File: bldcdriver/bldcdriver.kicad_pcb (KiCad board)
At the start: 2 copper layers, 147.3 x 81.3 mm, 2 parts, among them U1 DRV8304HRHAR, U2 STM32F103C8Tx

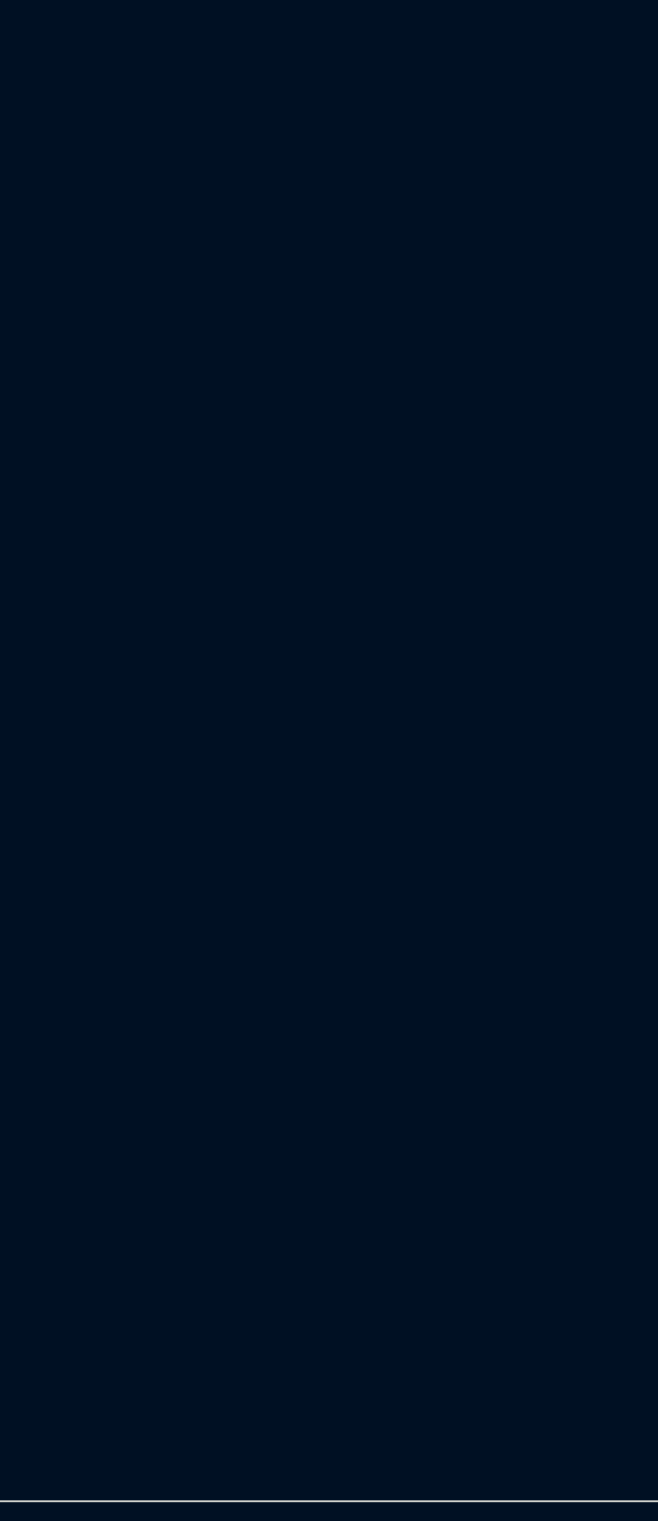
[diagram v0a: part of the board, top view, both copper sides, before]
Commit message: Finished N MOSFET Triple Half Bridge Circuit with Global Labels, looking if I want to use a P MOSFET
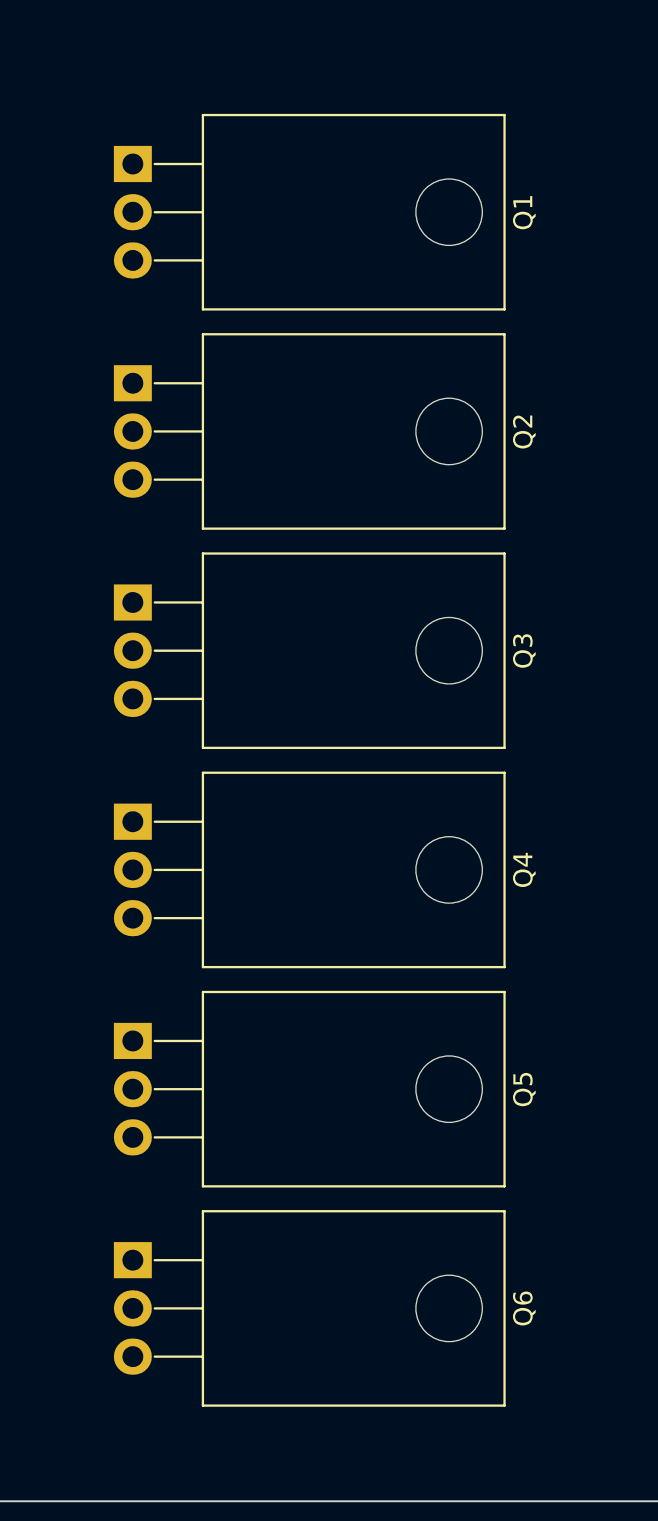
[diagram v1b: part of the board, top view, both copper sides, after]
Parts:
- added Q1: IRF3205, Package_TO_SOT_THT:TO-220-3_Horizontal_TabDown, F.Cu at (135.6, 61.6)
- added Q2: IRF3205, Package_TO_SOT_THT:TO-220-3_Horizontal_TabDown, F.Cu at (135.6, 73.2)
- added Q3: IRF3205, Package_TO_SOT_THT:TO-220-3_Horizontal_TabDown, F.Cu at (135.6, 84.7)
- added Q4: IRF3205, Package_TO_SOT_THT:TO-220-3_Horizontal_TabDown, F.Cu at (135.6, 96.3)
- added Q5: IRF3205, Package_TO_SOT_THT:TO-220-3_Horizontal_TabDown, F.Cu at (135.6, 107.8)
- added Q6: IRF3205, Package_TO_SOT_THT:TO-220-3_Horizontal_TabDown, F.Cu at (135.6, 119.4)
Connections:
- U1 pad 13: unconnected-(U1-GLB-Pad13) -> GLB
- U1 pad 14: unconnected-(U1-SHB-Pad14) -> SHB
- U1 pad 15: unconnected-(U1-GHB-Pad15) -> GHB
- U1 pad 16: unconnected-(U1-GHC-Pad16) -> GHC
- U1 pad 17: unconnected-(U1-SHC-Pad17) -> SHC
- U1 pad 18: unconnected-(U1-GLC-Pad18) -> GLC
- U1 pad 6: unconnected-(U1-GHA-Pad6) -> GHA
- U1 pad 7: unconnected-(U1-SHA-Pad7) -> SHA
- U1 pad 8: unconnected-(U1-GLA-Pad8) -> GLA

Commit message: Few more connections and capacitors
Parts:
- added R1: R, Resistor_SMD:R_0201_0603Metric, F.Cu at (98.7, 100.6)
- added R2: R, Resistor_SMD:R_0201_0603Metric, F.Cu at (98.7, 102.4)
- added R3: R, Resistor_SMD:R_0201_0603Metric, F.Cu at (98.7, 104.1)
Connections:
- net SHA renamed PHASEA
- net SHB renamed PHASEB
- net SHC renamed PHASEC
- Q1 pad 2: unconnected-(Q1-D-Pad2) -> VCC
- Q2 pad 3: unconnected-(Q2-S-Pad3) -> SPA
- Q3 pad 2: unconnected-(Q3-D-Pad2) -> VCC
- Q4 pad 3: unconnected-(Q4-S-Pad3) -> SPB
- Q5 pad 2: unconnected-(Q5-D-Pad2) -> VCC
- Q6 pad 3: unconnected-(Q6-S-Pad3) -> SPC
- U1 pad 1: unconnected-(U1-CPL-Pad1) -> Net-(U1-CPL)
- U1 pad 10: unconnected-(U1-SNA-Pad10) -> SNA
- U1 pad 11: unconnected-(U1-SNB-Pad11) -> SNA
- U1 pad 12: unconnected-(U1-SPB-Pad12) -> SPB
- U1 pad 19: unconnected-(U1-SPC-Pad19) -> SPC
- U1 pad 2: unconnected-(U1-CPH-Pad2) -> Net-(U1-CPH)
- U1 pad 20: unconnected-(U1-SNC-Pad20) -> SNA
- U1 pad 24: unconnected-(U1-VREF-Pad24) -> VCC
- U1 pad 32: unconnected-(U1-AGND-Pad32) -> SNA
- U1 pad 4: unconnected-(U1-VM-Pad4) -> VCC
- U1 pad 40: unconnected-(U1-PGND-Pad40) -> SNA
- U1 pad 41: unconnected-(U1-PAD-Pad41) -> SNA
- U1 pad 5: unconnected-(U1-VDRAIN-Pad5) -> VCC
- U1 pad 9: unconnected-(U1-SPA-Pad9) -> SPA

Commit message: Few changes, not sure
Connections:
- U1 pad 24: VCC -> unconnected-(U1-VREF-Pad24)
- U1 pad 33: unconnected-(U1-DVDD-Pad33) -> +3.3V
- U2 pad 1: unconnected-(U2-VBAT-Pad1) -> VCC
- U2 pad 23: Net-(U2-VSS-Pad23) -> SNA
- U2 pad 24: unconnected-(U2-VDD-Pad24) -> VCC
- U2 pad 35: Net-(U2-VSS-Pad23) -> SNA
- U2 pad 36: unconnected-(U2-VDD-Pad36) -> VCC
- U2 pad 47: Net-(U2-VSS-Pad23) -> SNA
- U2 pad 48: unconnected-(U2-VDD-Pad48) -> VCC
- U2 pad 8: unconnected-(U2-VSSA-Pad8) -> SNA
- U2 pad 9: unconnected-(U2-VDDA-Pad9) -> VCC

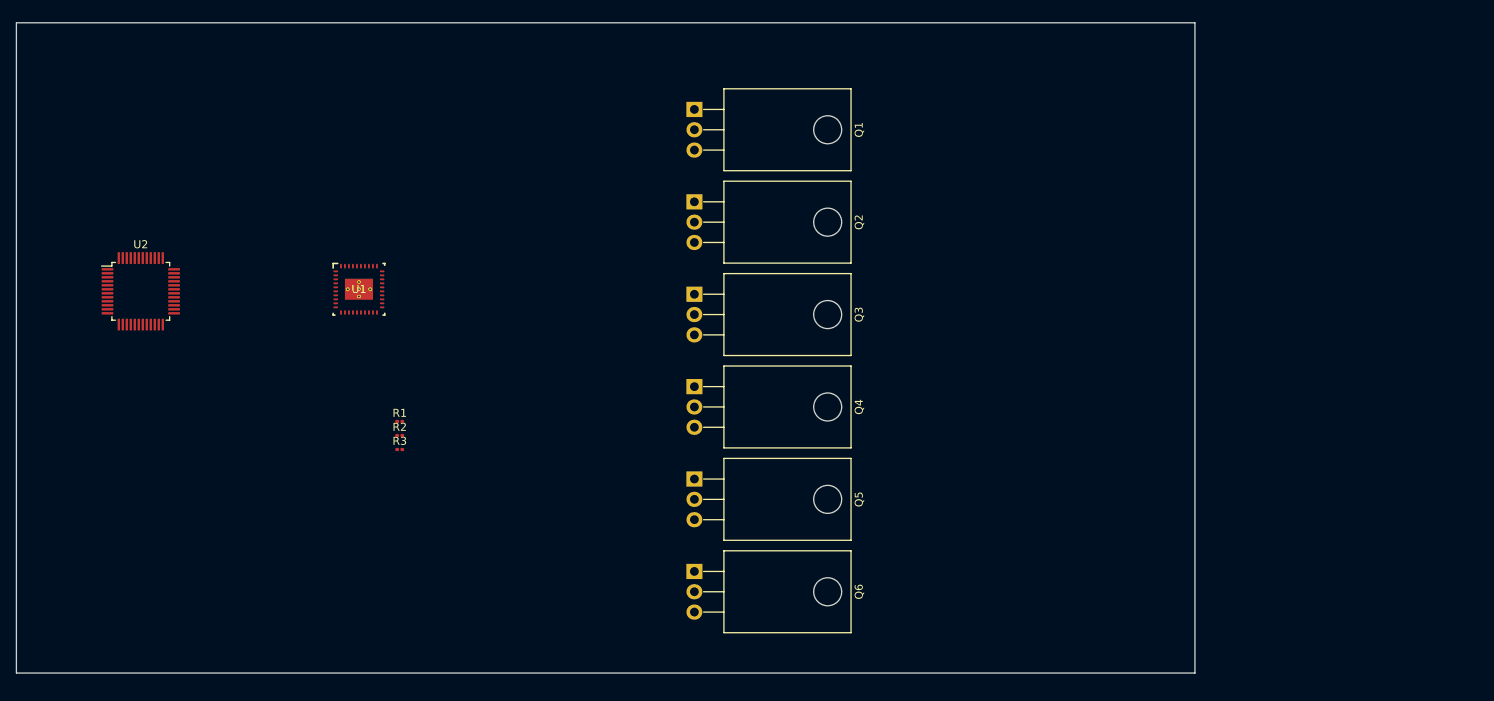
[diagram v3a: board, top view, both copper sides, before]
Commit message: Replaced STM32 with RP2040
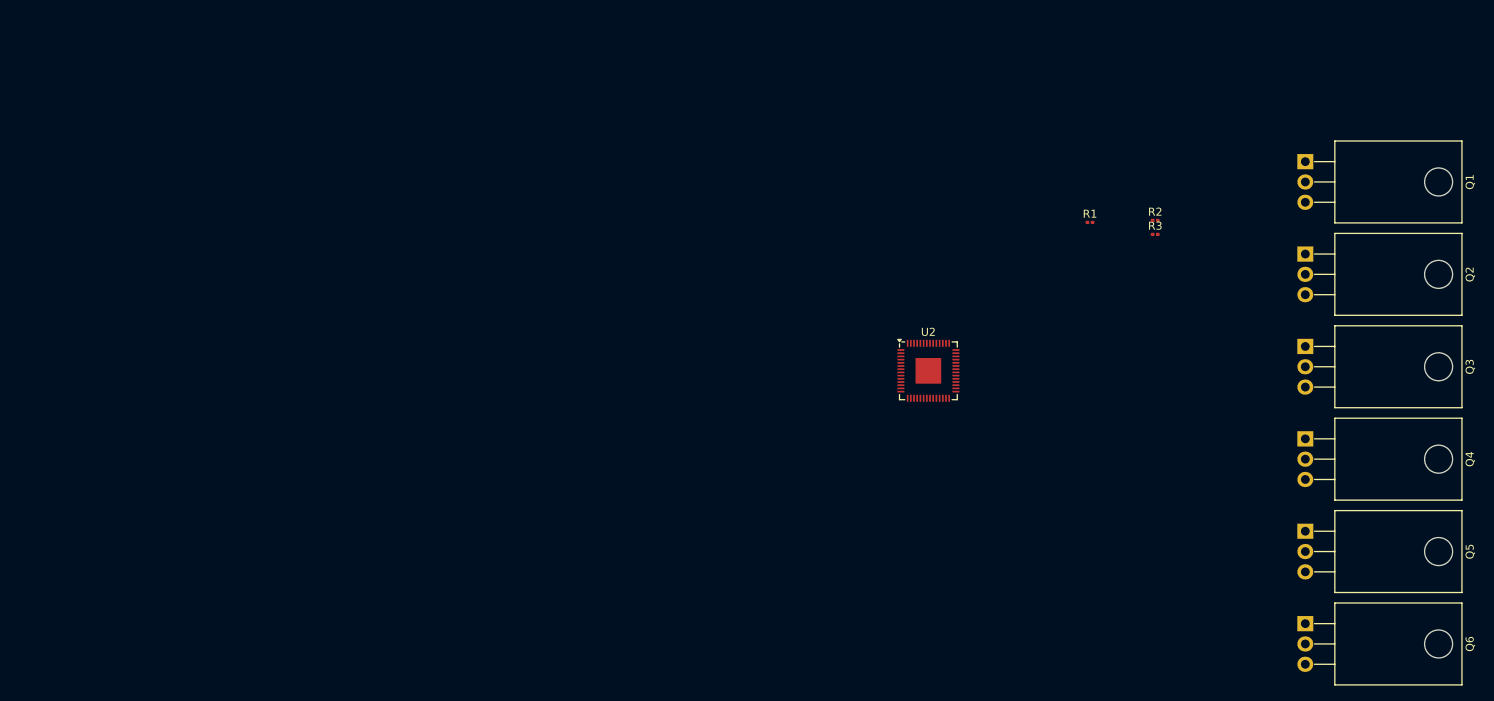
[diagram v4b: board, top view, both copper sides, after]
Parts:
- removed U1: DRV8304HRHAR, DRV8304:RHA0040E
- U2: value STM32F103C8Tx -> RP2040; footprint Package_QFP:LQFP-48_7x7mm_P0.5mm -> Package_DFN_QFN:QFN-56-1EP_7x7mm_P0.4mm_EP3.2x3.2mm
- moved U2 99.0 mm to (164.8, 94.3)
- moved R2 98.2 mm to (193.2, 75.5)
- moved R3 98.2 mm to (193.2, 77.2)
- moved R1 89.8 mm to (185.0, 75.8)
- moved Q1 76.6 mm to (211.9, 68.2)
- moved Q2 76.6 mm to (211.9, 79.7)
- moved Q3 76.6 mm to (211.9, 91.3)
- moved Q4 76.6 mm to (211.9, 102.8)
- moved Q5 76.6 mm to (211.9, 114.4)
- moved Q6 76.6 mm to (211.9, 125.9)
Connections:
- Q1 pad 2: VCC -> +24V
- Q3 pad 2: VCC -> +24V
- Q5 pad 2: VCC -> +24V
- U2 pad 1: VCC -> Net-(U2-IOVDD-Pad1)
- U2 pad 10: unconnected-(U2-PA0-Pad10) -> Net-(U2-IOVDD-Pad1)
- U2 pad 22: unconnected-(U2-PB11-Pad22) -> Net-(U2-IOVDD-Pad1)
- U2 pad 23: SNA -> Net-(U2-DVDD-Pad23)
- U2 pad 24: VCC -> unconnected-(U2-SWCLK-Pad24)
- U2 pad 33: unconnected-(U2-PA12-Pad33) -> Net-(U2-IOVDD-Pad1)
- U2 pad 35: SNA -> unconnected-(U2-GPIO23-Pad35)
- U2 pad 36: VCC -> unconnected-(U2-GPIO24-Pad36)
- U2 pad 42: unconnected-(U2-PB6-Pad42) -> Net-(U2-IOVDD-Pad1)
- U2 pad 47: SNA -> unconnected-(U2-USB_DP-Pad47)
- U2 pad 48: VCC -> unconnected-(U2-USB_VDD-Pad48)
- U2 pad 8: SNA -> unconnected-(U2-GPIO6-Pad8)
- U2 pad 9: VCC -> unconnected-(U2-GPIO7-Pad9)
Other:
- board outline removed

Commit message: Replaced the mistake in symbol from H to S, redid the connections, cleaned up local library folders, added proper net labels
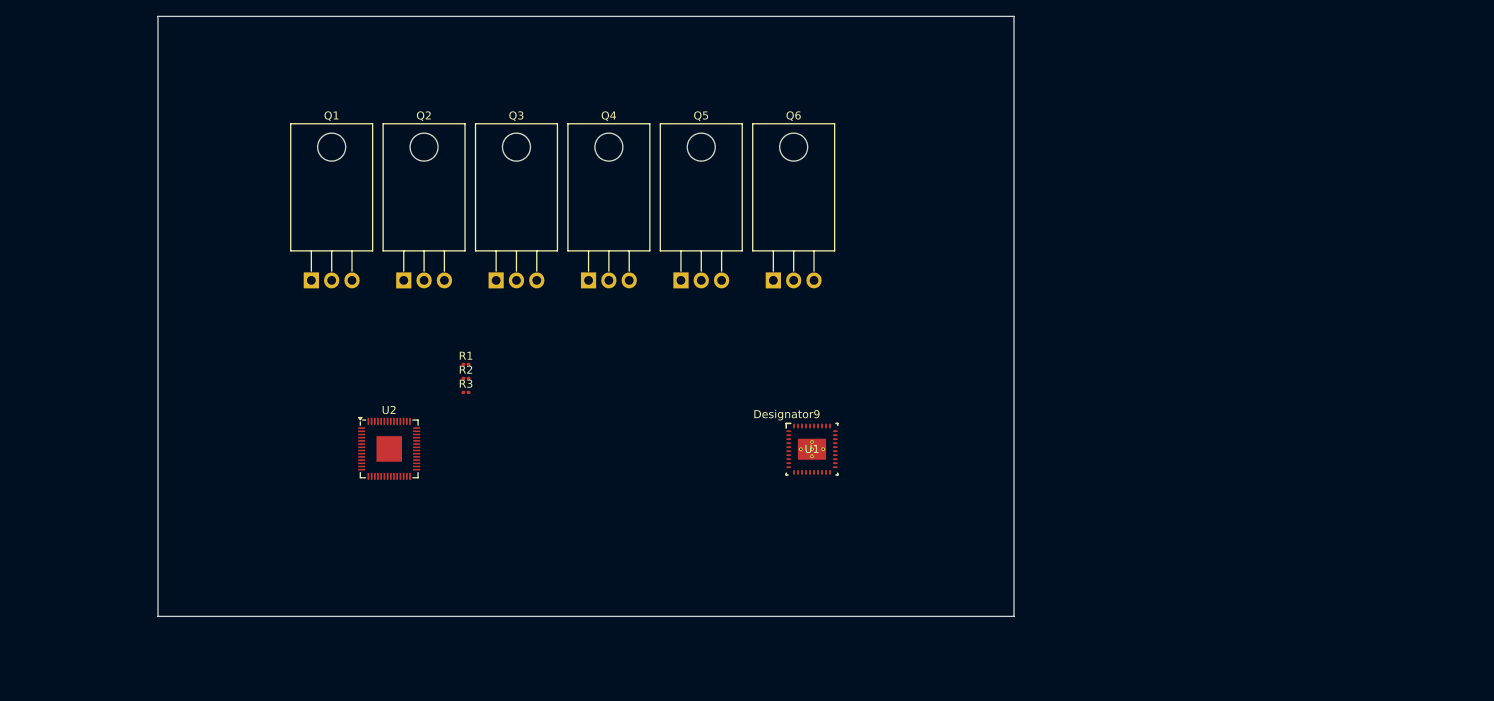
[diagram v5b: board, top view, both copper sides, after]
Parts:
- added U1: DRV8304SRHAR, DRV8304S:RHA0040E, F.Cu at (150.2, 104.1)
- moved Q1 125.1 mm to (87.7, 83.0), turned to 0 degrees
- moved Q2 112.7 mm to (99.2, 83.0), turned to 0 degrees
- moved Q3 101.5 mm to (110.8, 83.0), turned to 0 degrees
- moved Q4 91.8 mm to (122.3, 83.0), turned to 0 degrees
- moved R2 88.4 mm to (107.0, 95.2)
- moved R3 88.4 mm to (107.0, 97.0)
- moved Q5 84.1 mm to (133.9, 83.0), turned to 0 degrees
- moved R1 80.0 mm to (107.0, 93.5)
- moved Q6 79.1 mm to (145.4, 83.0), turned to 0 degrees
- moved U2 68.1 mm to (97.4, 104.1)
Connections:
- net PHASEA renamed /Phase A
- net PHASEB renamed /Phase B
- net PHASEC renamed /Phase C
- net SNA renamed GND
- net SPA renamed /SPA
- net SPB renamed /SPB
- net SPC renamed /SPC
- Q1 pad 1: GHA -> /GHA
- Q2 pad 1: GLA -> /GLA
- Q3 pad 1: GHB -> /GHB
- Q4 pad 1: GLB -> /GLB
- Q5 pad 1: GHC -> /GHC
- Q6 pad 1: GLC -> /GLC
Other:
- board outline added: 107 x 75 mm
